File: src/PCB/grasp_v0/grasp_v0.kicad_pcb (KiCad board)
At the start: 2 copper layers, 4 parts, among them U1 Pico, U2 LM1117T-3.3

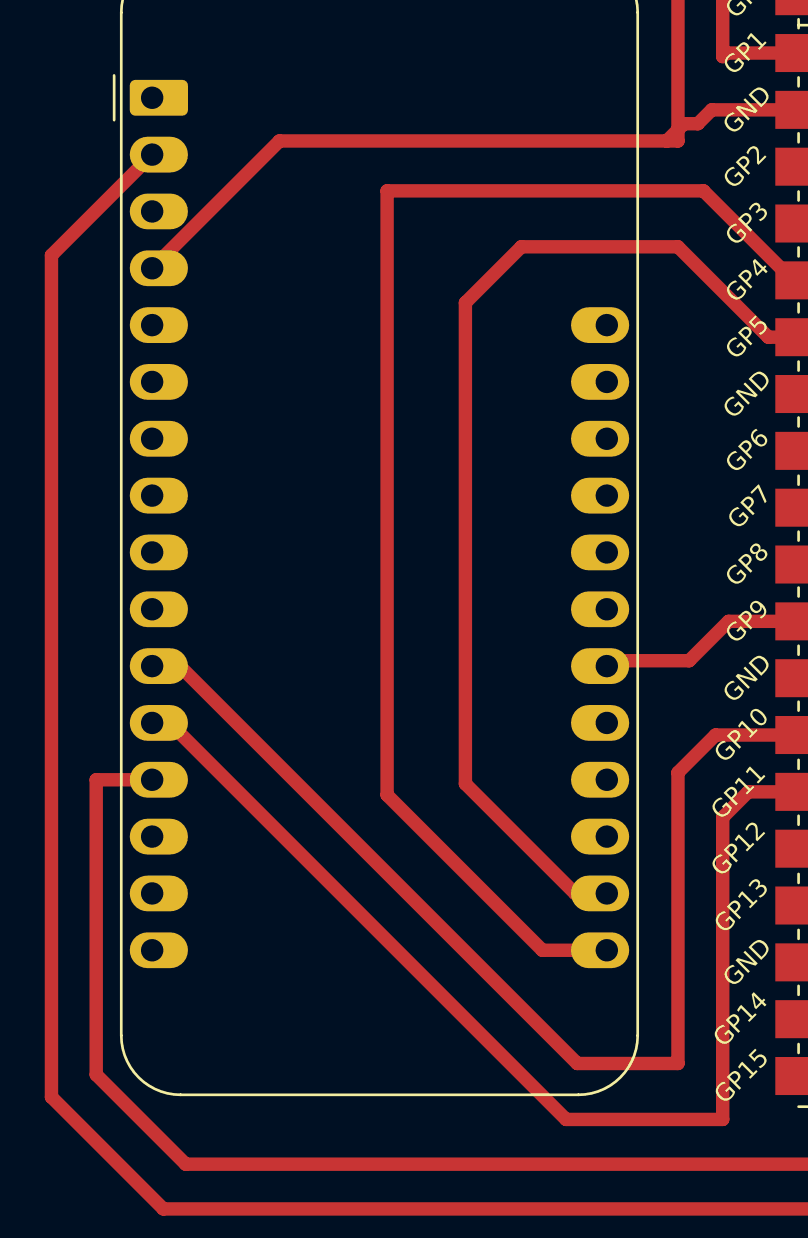
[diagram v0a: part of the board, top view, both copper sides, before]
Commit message: Folder reorg + new PCB and SPICE files
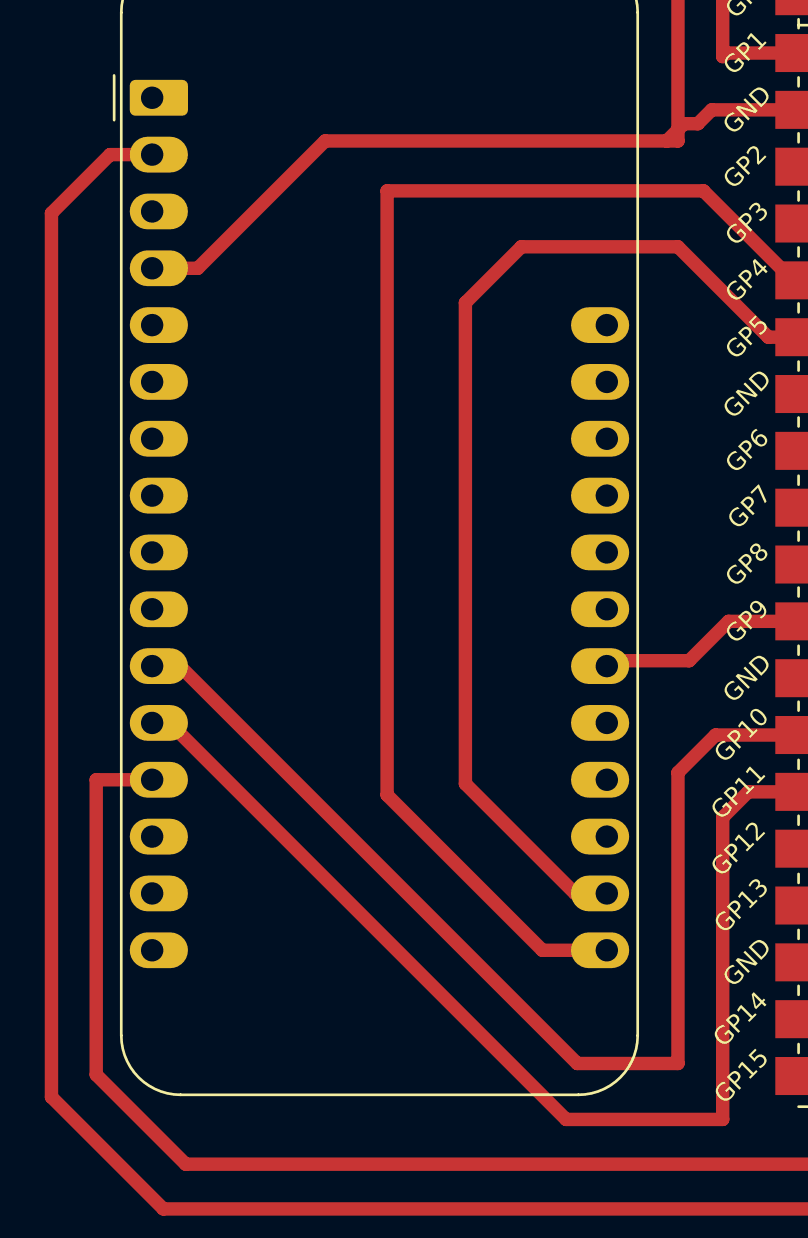
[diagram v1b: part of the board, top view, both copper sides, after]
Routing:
- net Net-(A1-3V3): track 119.8 -> 120.9 mm
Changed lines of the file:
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@@
-	)
-	(segment
-		(start 68.19 42.77)
-		(end 85.5 42.77)
-		(width 0.6)
-		(layer "F.Cu")
-		(net 56)
 	)
 	(segment
@@
 	)
 	(segment
-		(start 62.5 48.46)
-		(end 68.19 42.77)
-		(width 0.6)
-		(layer "F.Cu")
-		(net 56)
-	)
-	(segment
 		(start 85.5 42.77)
 		(end 86.27 42)
@@
 	)
 	(segment
+		(start 62.5 48.46)
+		(end 64.54 48.46)
+		(width 0.6)
+		(layer "F.Cu")
+		(net 56)
+	)
+	(segment
+		(start 70.23 42.77)
+		(end 85.5 42.77)
+		(width 0.6)
+		(layer "F.Cu")
+		(net 56)
+	)
+	(segment
 		(start 160 48)
 		(end 160 62.5)
@@
 	)
 	(segment
-		(start 114.5 90.5)
-		(end 123.54 81.46)
+		(start 64.54 48.46)
+		(end 70.23 42.77)
+		(width 0.6)
+		(layer "F.Cu")
+		(net 56)
+	)
+	(segment
+		(start 60.62 43.38)
+		(end 58 46)
 		(width 0.6)
 		(layer "F.Cu")
@@
 	)
 	(segment
-		(start 62.5 43.38)
-		(end 58 47.88)
+		(start 63 90.5)
+		(end 114.5 90.5)
 		(width 0.6)
 		(layer "F.Cu")
@@
 	)
 	(segment
-		(start 58 47.88)
+		(start 58 46)
 		(end 58 85.5)
+		(width 0.6)
+		(layer "F.Cu")
+		(net 57)
+	)
+	(segment
+		(start 114.5 90.5)
+		(end 123.54 81.46)
+		(width 0.6)
+		(layer "F.Cu")
+		(net 57)
+	)
+	(segment
+		(start 62.5 43.38)
+		(end 60.62 43.38)
 		(width 0.6)
 		(layer "F.Cu")
@@
 		(width 0.6)
 		(layer "F.Cu")
-		(net 57)
-	)
-	(segment
-		(start 63 90.5)
-		(end 114.5 90.5)
-		(width 0.6)
-		(layer "F.Cu")
